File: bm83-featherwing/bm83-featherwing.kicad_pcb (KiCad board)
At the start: 2 copper layers, 33 x 50.8 mm, 1 part, among them U1 BM83SM1-00AA

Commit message: BM83 work
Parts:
- added ?: , , F.Cu at (137.2, 72.4)
- added C1: 1uF, Capacitor_SMD:C_0805_2012Metric_Pad1.18x1.45mm_HandSolder, F.Cu at (196.8, 114.3)
- added C2: 1uF, Capacitor_SMD:C_0805_2012Metric_Pad1.18x1.45mm_HandSolder, F.Cu at (186.4, 126.5)
- added C3: 0.1uF, Capacitor_SMD:C_0805_2012Metric_Pad1.18x1.45mm_HandSolder, F.Cu at (186.4, 123.5)
- added C4: 0.1uF, Capacitor_SMD:C_0805_2012Metric_Pad1.18x1.45mm_HandSolder, F.Cu at (201.9, 111.3)
- added D1: PESD5V0S1BA, Diode_SMD:D_SOD-323_HandSoldering, F.Cu at (191.6, 117.5)
- added D2: PESD5V0S1BA, Diode_SMD:D_SOD-323_HandSoldering, F.Cu at (186.5, 117.5)
- added D3: SMBJ10CA, Diode_SMD:D_SMB_Handsoldering, F.Cu at (179.0, 112.6)
- added D4: LED_Small, LED_SMD:LED_0805_2012Metric_Pad1.15x1.40mm_HandSolder, F.Cu at (196.5, 117.6)
- added D5: LED_Small, LED_SMD:LED_0805_2012Metric_Pad1.15x1.40mm_HandSolder, F.Cu at (191.5, 120.5)
- added D6: D_TVS, Diode_SMD:D_SOD-323_HandSoldering, F.Cu at (186.5, 120.5)
- added D7: D_TVS, Diode_SMD:D_SOD-323_HandSoldering, F.Cu at (197.0, 111.3)
- added J1: TOP, Footprints:RoundPinHeader_1x12, F.Cu at (135.9, 111.8)
- added J2: BOT, Footprints:RoundPinHeader_1x16, F.Cu at (156.2, 83.8)
- added J3: DX07S016JA1R1500, Footprints:JAE_DX07S016JA1R1500, F.Cu at (146.3, 123.4)
- added R1: 5.1K, Resistor_SMD:R_0805_2012Metric_Pad1.20x1.40mm_HandSolder, F.Cu at (201.6, 114.3)
- added R2: 5.1K, Resistor_SMD:R_0805_2012Metric_Pad1.20x1.40mm_HandSolder, F.Cu at (191.2, 126.5)
- added R3: 4.7K, Resistor_SMD:R_0805_2012Metric_Pad1.20x1.40mm_HandSolder, F.Cu at (191.2, 123.5)
- added REF**: MountingHole_2.7mm_M2.5_ISO14580_Pad, MountingHole:MountingHole_2.7mm_M2.5_ISO14580_Pad, F.Cu at (154.9, 125.7)
- added REF**: MountingHole_2.7mm_M2.5_ISO14580_Pad, MountingHole:MountingHole_2.7mm_M2.5_ISO14580_Pad, F.Cu at (137.2, 72.4)
- added REF**: MountingHole_2.7mm_M2.5_ISO14580_Pad, MountingHole:MountingHole_2.7mm_M2.5_ISO14580_Pad, F.Cu at (154.9, 72.4)
- added REF**: MountingHole_2.7mm_M2.5_ISO14580_Pad, MountingHole:MountingHole_2.7mm_M2.5_ISO14580_Pad, F.Cu at (137.2, 125.7)
- added SW1: Reset Switch, Footprints:PTS636SK25SMTRLFS, F.Cu at (189.3, 112.9)
- added SW2: Power Switch, Footprints:PTS636SK25SMTRLFS, F.Cu at (178.9, 124.7)
- added SW3: Config Switch, Footprints:PTS636SK25SMTRLFS, F.Cu at (178.9, 118.5)
- moved U1 6.86 mm to (138.4, 107.4)
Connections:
- U1 pad 1: no_connect_(U1-Pad1) -> unconnected-(U1-Pad1)
- U1 pad 10: no_connect_(U1-Pad10) -> unconnected-(U1-Pad10)
- U1 pad 11: no_connect_(U1-Pad11) -> unconnected-(U1-Pad11)
- U1 pad 12: no_connect_(U1-Pad12) -> unconnected-(U1-Pad12)
- U1 pad 13: no_connect_(U1-Pad13) -> unconnected-(U1-Pad13)
- U1 pad 14: no_connect_(U1-Pad14) -> unconnected-(U1-Pad14)
- U1 pad 15: no_connect_(U1-Pad15) -> unconnected-(U1-Pad15)
- U1 pad 17: no_connect_(U1-Pad17) -> unconnected-(U1-Pad17)
- U1 pad 18: no_connect_(U1-Pad18) -> unconnected-(U1-Pad18)
- U1 pad 19: no_connect_(U1-Pad19) -> unconnected-(U1-Pad19)
- U1 pad 2: no_connect_(U1-Pad2) -> LRCK
- U1 pad 20: no_connect_(U1-Pad20) -> unconnected-(U1-Pad20)
- U1 pad 21: no_connect_(U1-Pad21) -> unconnected-(U1-Pad21)
- U1 pad 22: no_connect_(U1-Pad22) -> ADAP_IN
- U1 pad 23: no_connect_(U1-Pad23) -> +3V3
- U1 pad 24: no_connect_(U1-Pad24) -> SYS_PWR
- U1 pad 25: no_connect_(U1-Pad25) -> VDD_IO
- U1 pad 26: no_connect_(U1-Pad26) -> MFB
- U1 pad 27: no_connect_(U1-Pad27) -> unconnected-(U1-Pad27)
- U1 pad 28: no_connect_(U1-Pad28) -> unconnected-(U1-Pad28)
- U1 pad 29: no_connect_(U1-Pad29) -> RXD
- U1 pad 3: no_connect_(U1-Pad3) -> SCK
- U1 pad 30: no_connect_(U1-Pad30) -> TXD
- U1 pad 31: no_connect_(U1-Pad31) -> P3_4
- U1 pad 32: no_connect_(U1-Pad32) -> LED1
- U1 pad 33: no_connect_(U1-Pad33) -> unconnected-(U1-Pad33)
- U1 pad 34: no_connect_(U1-Pad34) -> LED2
- U1 pad 35: no_connect_(U1-Pad35) -> unconnected-(U1-Pad35)
- U1 pad 36: no_connect_(U1-Pad36) -> USB_DM
- U1 pad 37: no_connect_(U1-Pad37) -> USB_DP
- U1 pad 38: no_connect_(U1-Pad38) -> unconnected-(U1-Pad38)
- U1 pad 39: no_connect_(U1-Pad39) -> unconnected-(U1-Pad39)
- U1 pad 4: no_connect_(U1-Pad4) -> SDI
- U1 pad 40: no_connect_(U1-Pad40) -> unconnected-(U1-Pad40)
- U1 pad 41: no_connect_(U1-Pad41) -> unconnected-(U1-Pad41)
- U1 pad 42: no_connect_(U1-Pad42) -> unconnected-(U1-Pad42)
- U1 pad 43: no_connect_(U1-Pad43) -> RST_N
- U1 pad 44: no_connect_(U1-Pad44) -> unconnected-(U1-Pad44)
- U1 pad 45: no_connect_(U1-Pad45) -> unconnected-(U1-Pad45)
- U1 pad 46: no_connect_(U1-Pad46) -> unconnected-(U1-Pad46)
- U1 pad 47: no_connect_(U1-Pad47) -> unconnected-(U1-Pad47)
- U1 pad 48: no_connect_(U1-Pad48) -> unconnected-(U1-Pad48)
- U1 pad 49: no_connect_(U1-Pad49) -> unconnected-(U1-Pad49)
- U1 pad 5: no_connect_(U1-Pad5) -> MCK
- U1 pad 6: no_connect_(U1-Pad6) -> unconnected-(U1-Pad6)
- U1 pad 7: no_connect_(U1-Pad7) -> unconnected-(U1-Pad7)
- U1 pad 8: no_connect_(U1-Pad8) -> unconnected-(U1-Pad8)
- U1 pad 9: no_connect_(U1-Pad9) -> unconnected-(U1-Pad9)
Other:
- board size 33 x 50.8 mm -> 33 x 59.4 mm

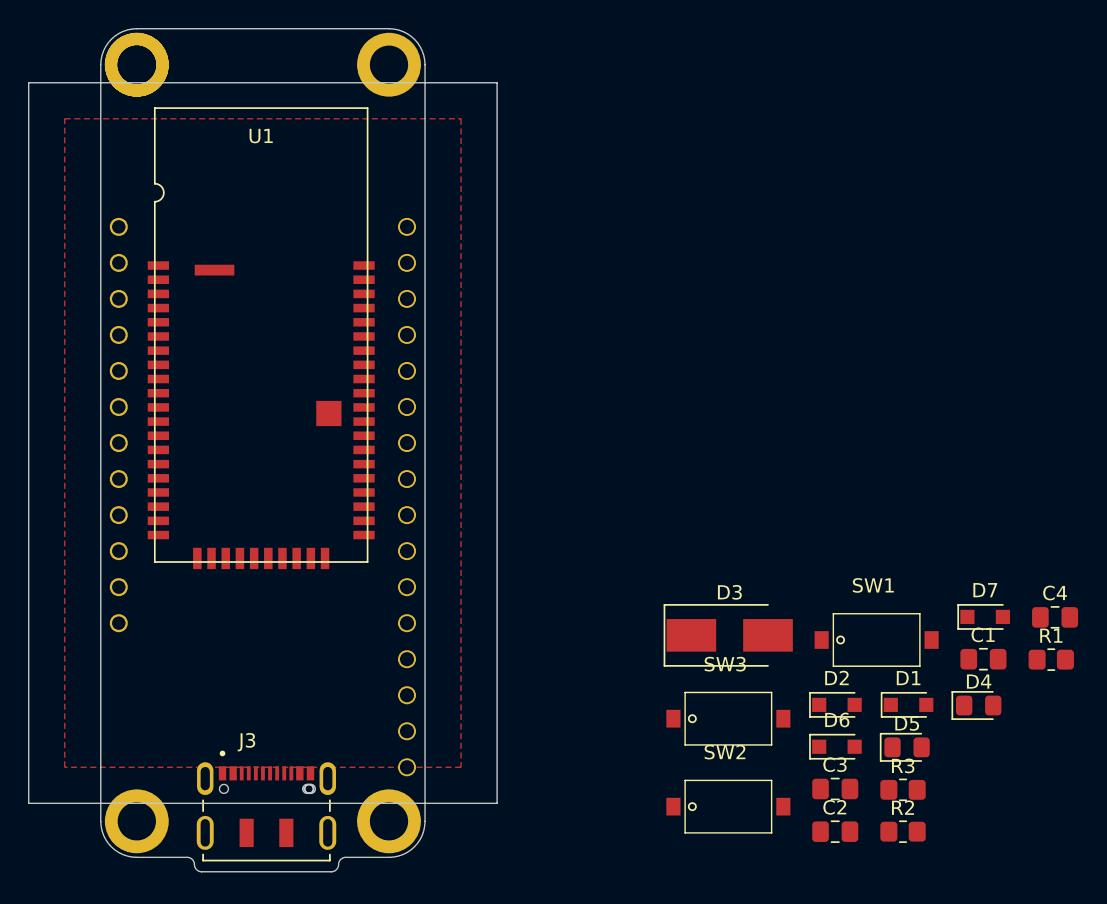
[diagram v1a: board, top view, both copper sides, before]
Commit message: BM83 SPST switch
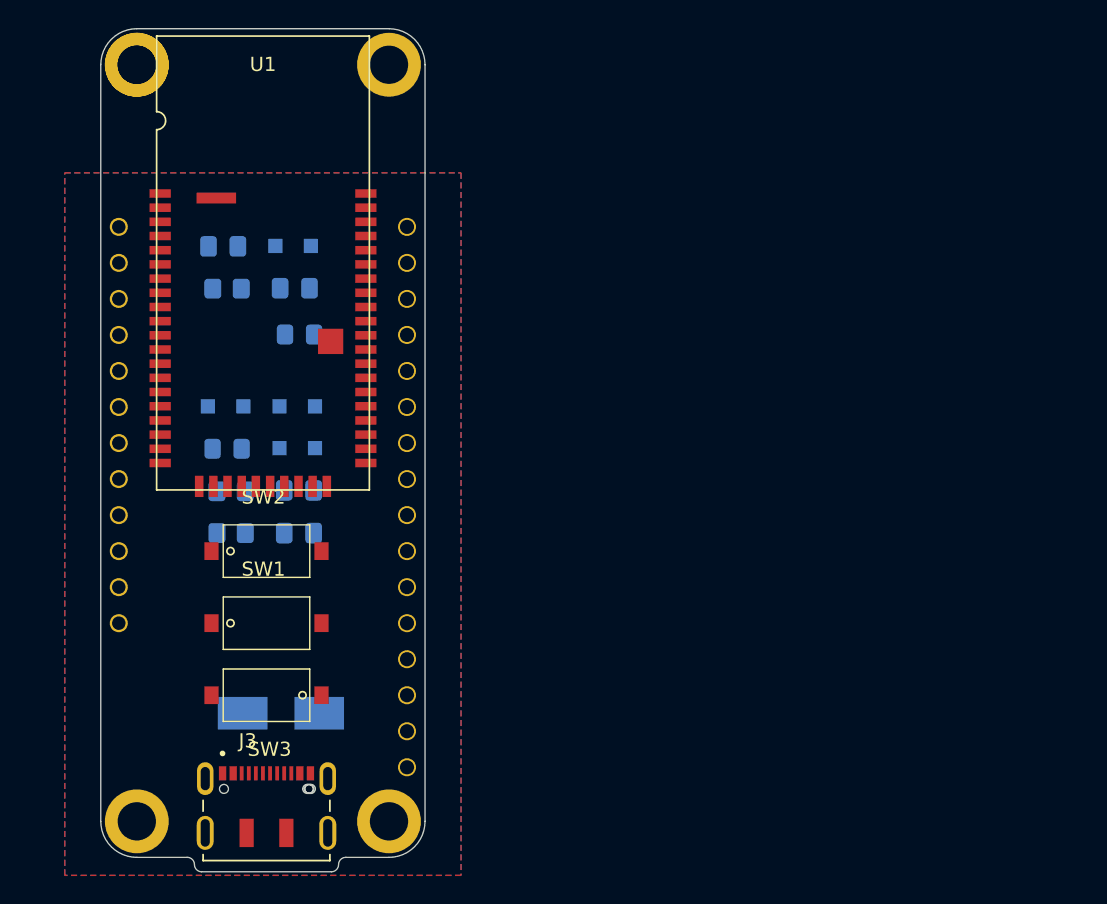
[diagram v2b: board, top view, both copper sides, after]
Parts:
- C1, C2, C3, C4, D1, D2, D3, D4, D5, D6, D7, R1, R2, R3: moved to B.Cu
- moved C4 64.2 mm to (143.2, 85.2), turned to 180 degrees
- moved R1 63.7 mm to (143.5, 88.2), turned to 180 degrees
- moved D7 55.4 mm to (148.2, 85.2), turned to 180 degrees
- moved C1 55.1 mm to (148.3, 88.1), turned to 180 degrees
- moved D4 54.6 mm to (148.6, 91.4), turned to 180 degrees
- moved D1 52.6 mm to (143.4, 96.5), turned to 180 degrees
- moved D5 52.4 mm to (143.5, 99.5), turned to 180 degrees
- moved R3 51.8 mm to (143.8, 102.5), turned to 180 degrees
- moved R2 51.8 mm to (143.8, 105.4), turned to 180 degrees
- moved D2 43.5 mm to (148.5, 96.5), turned to 180 degrees
- moved D6 43.5 mm to (148.5, 99.4), turned to 180 degrees
- moved C2 43.3 mm to (148.6, 105.4), turned to 180 degrees
- moved C3 43.3 mm to (148.6, 102.4), turned to 180 degrees
- moved SW1 43.0 mm to (146.3, 111.8)
- moved SW2 37.2 mm to (146.3, 106.7)
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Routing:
- added copper zone on B.Cu, net +3V3
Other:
- board size 33 x 59.4 mm -> 22.9 x 59.4 mm

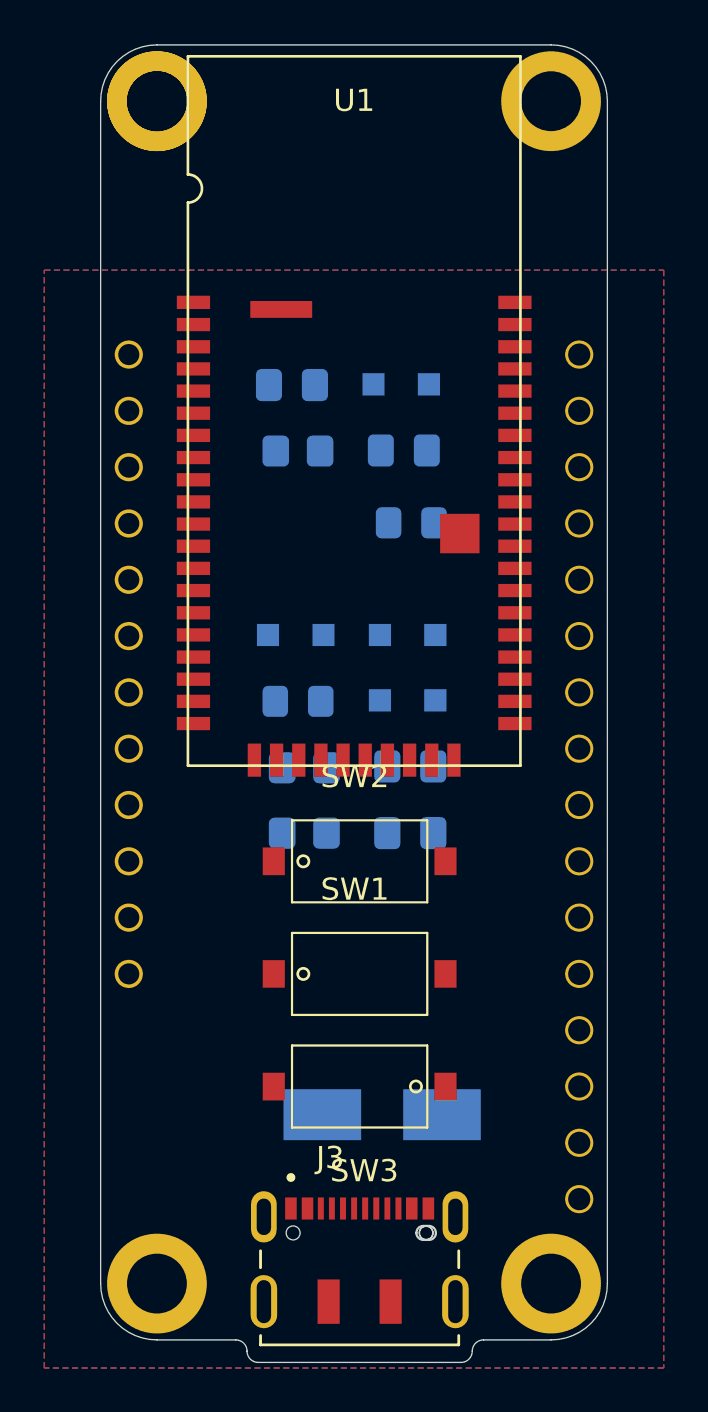
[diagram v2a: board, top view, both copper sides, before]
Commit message: BM83 board first route. Needs labelling
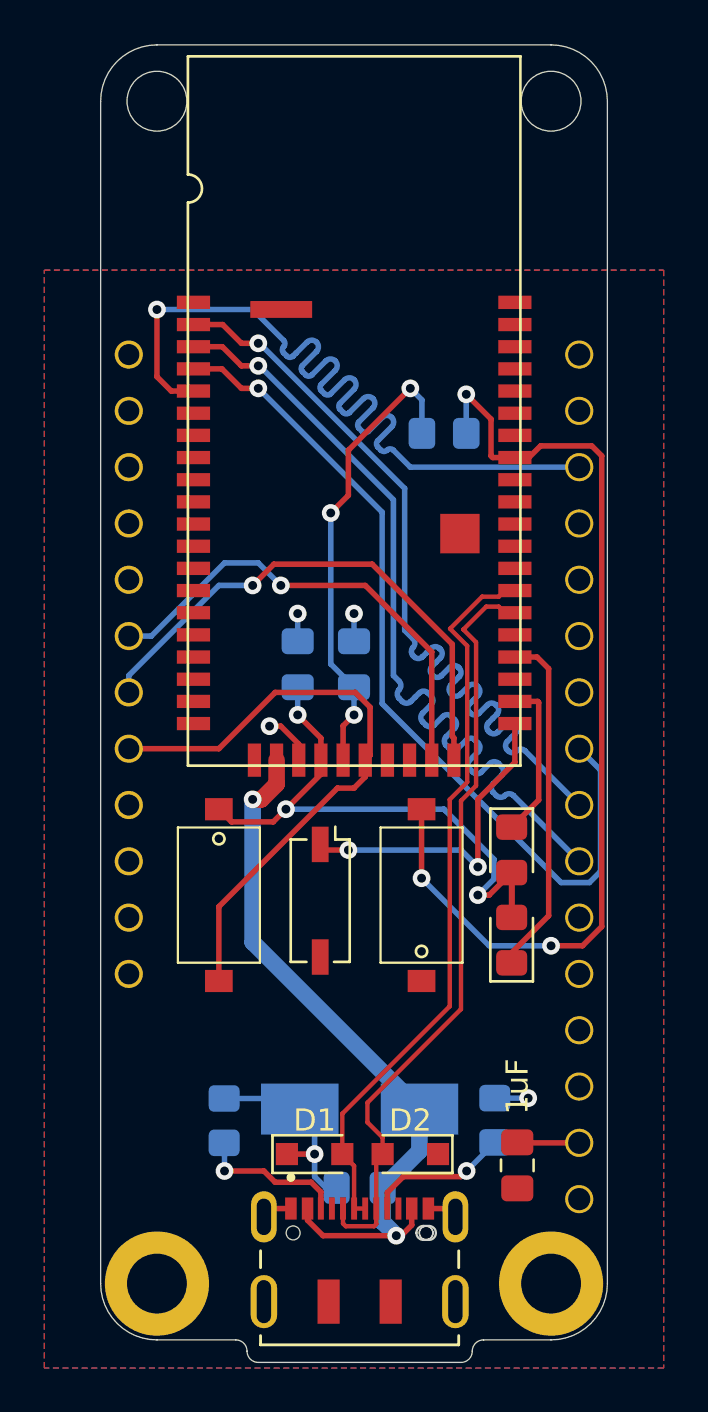
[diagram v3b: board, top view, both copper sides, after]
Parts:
- removed D6, D7: D_TVS, Diode_SMD:D_SOD-323_HandSoldering
- removed the REF** at (154.9, 125.7)
- removed the REF** at (137.2, 72.4)
- removed the REF** at (154.9, 72.4)
- removed the REF** at (137.2, 125.7)
- added REF**: MountingHole_2.7mm_M2.5_DIN965_Pad, MountingHole:MountingHole_2.7mm_M2.5_DIN965_Pad, F.Cu at (137.2, 125.7)
- added REF**: MountingHole_2.7mm_M2.5_DIN965, MountingHole:MountingHole_2.7mm_M2.5_DIN965, F.Cu at (154.9, 72.4)
- added REF**: MountingHole_2.7mm_M2.5_DIN965, MountingHole:MountingHole_2.7mm_M2.5_DIN965, F.Cu at (137.2, 72.4)
- C2, D1, D2, D4, D5: moved to F.Cu
- SW3: value Config Switch -> SW_DIP_x01; footprint Footprints:PTS636SK25SMTRLFS -> Button_Switch_SMD:SW_DIP_SPSTx01_Slide_Copal_CHS-01A_W5.08mm_P1.27mm_JPin
- moved ? 56.2 mm to (154.9, 125.7)
- moved C1 33.3 mm to (146.3, 121.4)
- moved R1 31.5 mm to (152.4, 118.4), turned to -90 degrees
- moved D1 23.4 mm to (144.3, 119.9), turned to 0 degrees
- moved D2 23.4 mm to (148.6, 119.9)
- moved R3 16.3 mm to (150.1, 87.4), turned to 0 degrees
- moved C2 15.7 mm to (153.4, 120.4), turned to -90 degrees
- moved D4 15.4 mm to (153.2, 106.2), turned to -90 degrees
- moved D5 14.5 mm to (153.2, 110.2), turned to 90 degrees
- moved R2 13.5 mm to (140.2, 118.4), turned to 90 degrees
- moved C4 12.6 mm to (143.5, 97.8), turned to 90 degrees
- moved SW3 8.57 mm to (144.5, 108.5), turned to -90 degrees
- moved SW2 6.53 mm to (140.0, 108.2), turned to -90 degrees
- moved C3 5.26 mm to (146.1, 97.8), turned to 90 degrees
- moved SW1 4.52 mm to (149.1, 108.2), turned to 90 degrees
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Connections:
- net USB_DM renamed USB_N
- net USB_DP renamed USB_P
- R1 pad 2: Net-(J3-Pad3) -> Net-(J3-Pad9)
- R2 pad 1: Net-(J3-Pad9) -> Net-(J3-Pad3)
- SW1 pad 1: RST_N -> GND
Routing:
- net RST_N: track 0.00 -> 44.5 mm, vias 0 -> 3
- net SDI: track 0.00 -> 39.2 mm, vias 0 -> 1
- net LRCK: track 0.00 -> 38.9 mm, vias 0 -> 1
- net SCK: track 0.00 -> 38.9 mm, vias 0 -> 1
- net MCK: track 0.00 -> 38.9 mm, vias 0 -> 1
- net USB_N: track 0.00 -> 34.6 mm
- net USB_P: track 0.00 -> 33.2 mm
- net ADAP_IN: track 0.00 -> 32.7 mm, vias 0 -> 2
- net SYS_PWR: track 0.00 -> 28.4 mm, vias 0 -> 3
- net MFB: track 0.00 -> 27.8 mm
- net TXD: track 0.00 -> 24.2 mm, vias 0 -> 1
- net RXD: track 0.00 -> 21.6 mm, vias 0 -> 1
- net VDD_IO: track 0.00 -> 21.1 mm, vias 0 -> 3
- net GND: track 0.00 -> 16.2 mm, vias 0 -> 4
- net LED2: track 0.00 -> 15.7 mm
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
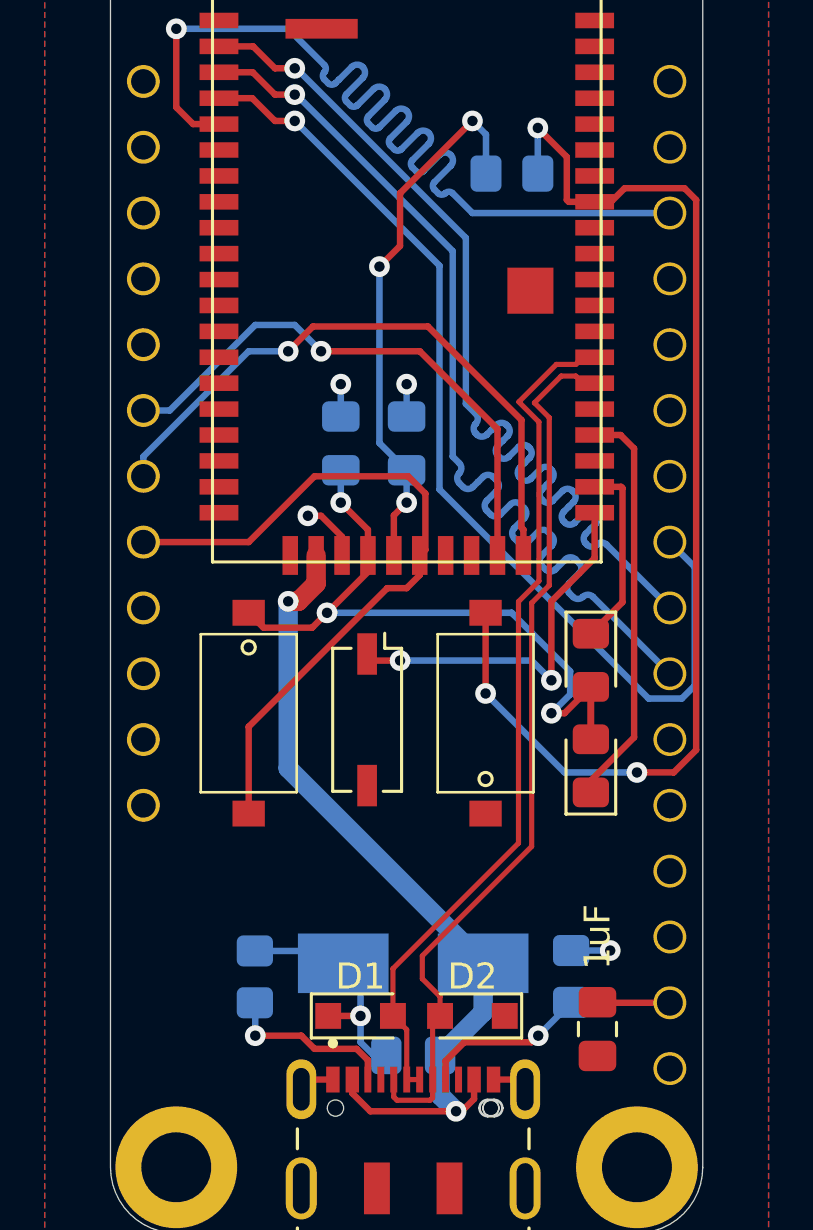
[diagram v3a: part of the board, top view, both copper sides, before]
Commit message: First gerber output for BM83
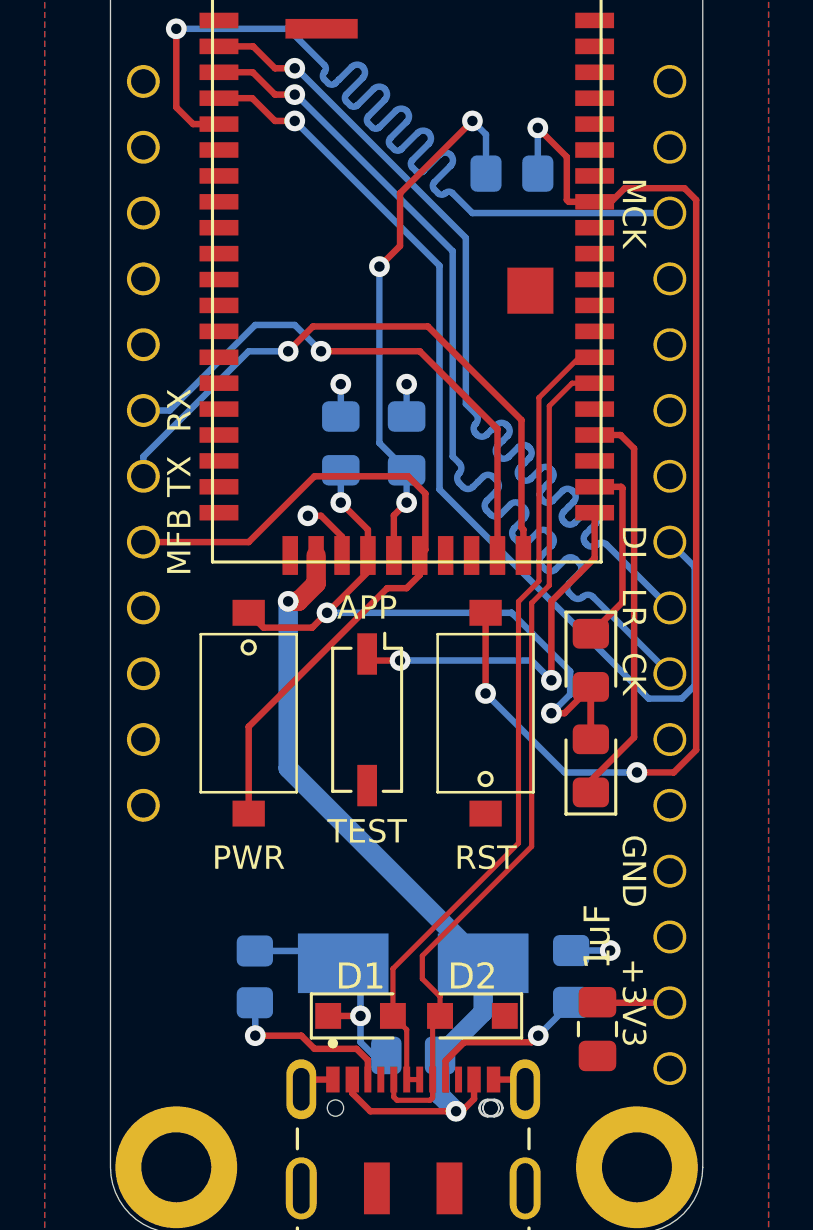
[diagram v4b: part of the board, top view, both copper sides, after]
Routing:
- net USB_N: track 34.6 -> 33.5 mm
- net USB_P: track 33.2 -> 32.2 mm
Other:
- board text added: "+3V3"
- board text added: "APP"
- board text added: "CK"
- board text added: "DI"
- board text added: "GND"
- board text added: "LR"
- board text added: "MCK"
- board text added: "MFB"
- board text added: "PWR"
- board text added: "RST"
- board text added: "RX"
- board text added: "TEST"
- board text added: "TX"
